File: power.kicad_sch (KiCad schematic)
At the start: 10 parts

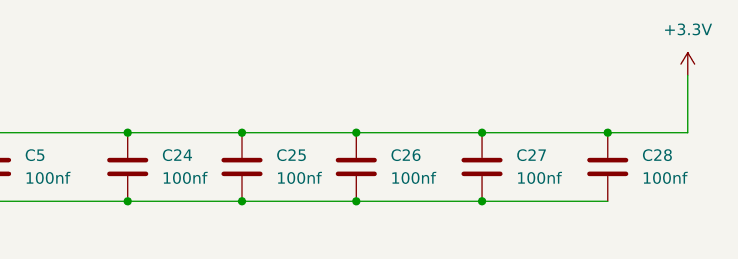
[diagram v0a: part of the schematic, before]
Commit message: feat: PCB layout updates, schematic changes, fp-lib-table config
- cnc_pic32.kicad_pcb: component repositioning, board outline, text formatting
- cnc_pic32.kicad_prl/pro: project settings updates
- fp-lib-table: add Library path to Library.pretty
- mcu.kicad_sch: PIC32 pin configuration updates
- zigbee.kicad_sch: MRF24J40 module updates
- oscilator.kicad_sch: crystal configuration
- power.kicad_sch/power_ft232.kicad_sch: power supply updates
- oled.kicad_sch: OLED display connections
- idc.kicad_sch: IDC connector updates
- osc_ft232.kicad_sch: FT232 crystal
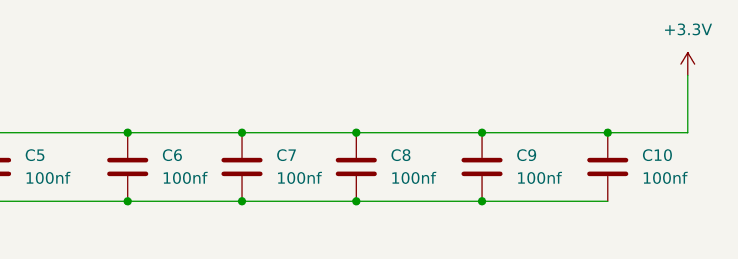
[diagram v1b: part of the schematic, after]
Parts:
- renumbered C28 to C10, C24 to C6, C25 to C7, C26 to C8, C27 to C9
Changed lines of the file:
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@@
 		(dnp no)
 		(fields_autoplaced yes)
-		(property "Reference" "C27"
+		(property "Reference" "C9"
 			(at 177.8 63.5 0)
 			(show_name no)
@@
 			(project "cnc_pic32"
 				(path "/13dbfc1f-be47-44ca-9042-3d6a9a657d7d/8e42f8aa-f00a-41b2-96fb-3753b4f2b509"
-					(reference "C27")
+					(reference "C9")
 					(unit 1)
 				)
@@
 		(dnp no)
 		(fields_autoplaced yes)
-		(property "Reference" "C24"
+		(property "Reference" "C6"
 			(at 138.43 63.5 0)
 			(show_name no)
@@
 			(project "cnc_pic32"
 				(path "/13dbfc1f-be47-44ca-9042-3d6a9a657d7d/8e42f8aa-f00a-41b2-96fb-3753b4f2b509"
-					(reference "C24")
+					(reference "C6")
 					(unit 1)
 				)
@@
 		(in_pos_files yes)
 		(dnp no)
-		(property "Reference" "#PWR040"
+		(property "Reference" "#PWR04"
 			(at 57.15 74.93 0)
 			(hide yes)
@@
 			(project "cnc_pic32"
 				(path "/13dbfc1f-be47-44ca-9042-3d6a9a657d7d/8e42f8aa-f00a-41b2-96fb-3753b4f2b509"
-					(reference "#PWR040")
+					(reference "#PWR04")
 					(unit 1)
 				)
@@
 		(dnp no)
 		(fields_autoplaced yes)
-		(property "Reference" "C26"
+		(property "Reference" "C8"
 			(at 163.83 63.5 0)
 			(show_name no)
@@
 			(project "cnc_pic32"
 				(path "/13dbfc1f-be47-44ca-9042-3d6a9a657d7d/8e42f8aa-f00a-41b2-96fb-3753b4f2b509"
-					(reference "C26")
+					(reference "C8")
 					(unit 1)
 				)
@@
 		(dnp no)
 		(fields_autoplaced yes)
-		(property "Reference" "#PWR039"
+		(property "Reference" "#PWR05"
 			(at 196.85 58.42 0)
 			(hide yes)
@@
 			(project "cnc_pic32"
 				(path "/13dbfc1f-be47-44ca-9042-3d6a9a657d7d/8e42f8aa-f00a-41b2-96fb-3753b4f2b509"
-					(reference "#PWR039")
+					(reference "#PWR05")
 					(unit 1)
 				)
@@
 		(dnp no)
 		(fields_autoplaced yes)
-		(property "Reference" "C25"
+		(property "Reference" "C7"
 			(at 151.13 63.5 0)
 			(show_name no)
@@
 			(project "cnc_pic32"
 				(path "/13dbfc1f-be47-44ca-9042-3d6a9a657d7d/8e42f8aa-f00a-41b2-96fb-3753b4f2b509"
-					(reference "C25")
+					(reference "C7")
 					(unit 1)
 				)
@@
 		(dnp no)
 		(fields_autoplaced yes)
-		(property "Reference" "C28"
+		(property "Reference" "C10"
 			(at 191.77 63.5 0)
 			(show_name no)
@@
 			(project "cnc_pic32"
 				(path "/13dbfc1f-be47-44ca-9042-3d6a9a657d7d/8e42f8aa-f00a-41b2-96fb-3753b4f2b509"
-					(reference "C28")
-					(unit 1)
-				)
+					(reference "C10")
+					(unit 1)
+				)

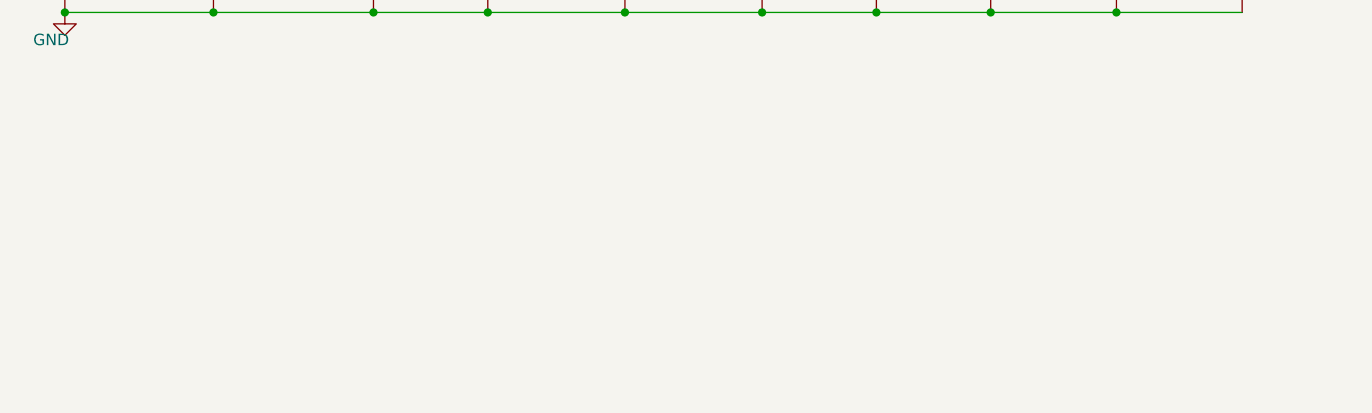
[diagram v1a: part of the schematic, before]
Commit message: feat: add orphaned PCB components to schematics - R4/R5 MCU, R41/R42 OLED, C37/C38 power
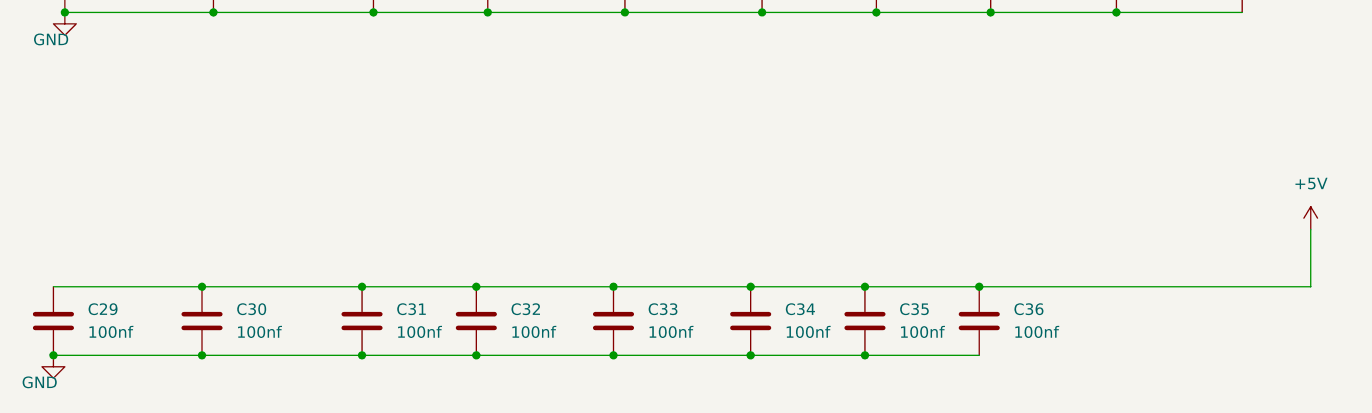
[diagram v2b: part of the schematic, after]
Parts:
- added C29, C30, C31, C32, C33, C34, C35, C36: 100nf, Capacitor_SMD:C_0805_2012Metric, symbol Device:C
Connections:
- net GND: now also C29.2, C30.2, C31.2, C32.2, C33.2, C34.2, C35.2, C36.2
- new net +5V: C29.1, C30.1, C31.1, C32.1, C33.1, C34.1, C35.1, C36.1

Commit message: feat: PCB layout updates, schematic changes, remove freerouting.dsn
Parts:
- removed C30: 100nf, Capacitor_SMD:C_0805_2012Metric, symbol Device:C
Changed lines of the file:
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@@
-	)
-	(junction
-		(at 72.39 106.68)
-		(diameter 0)
-		(color 0 0 0 0)
 	)
 	(junction
@@
 	)
 	(junction
-		(at 72.39 99.06)
-		(diameter 0)
-		(color 0 0 0 0)
-	)
-	(junction
 		(at 187.96 60.96)
 		(diameter 0)
@@
 	(wire
 		(pts
-			(xy 72.39 106.68) (xy 90.17 106.68)
+			(xy 55.88 106.68) (xy 90.17 106.68)
 		)
 		(stroke
@@
 	(wire
 		(pts
-			(xy 72.39 99.06) (xy 90.17 99.06)
+			(xy 55.88 99.06) (xy 90.17 99.06)
 		)
 		(stroke
@@
 	(wire
 		(pts
-			(xy 55.88 99.06) (xy 72.39 99.06)
-		)
-		(stroke
-			(width 0)
-			(type default)
-		)
-	)
-	(wire
-		(pts
 			(xy 73.66 60.96) (xy 91.44 60.96)
-		)
-		(stroke
-			(width 0)
-			(type default)
-		)
-	)
-	(wire
-		(pts
-			(xy 55.88 106.68) (xy 72.39 106.68)
 		)
 		(stroke
@@
 					(unit 1)
 				)
-			)
-		)
-	)
-	(symbol
-		(lib_name "C_1")
-		(lib_id "Device:C")
-		(at 72.39 102.87 0)
-		(unit 1)
-		(body_style 1)
-		(exclude_from_sim no)
-		(in_bom yes)
-		(on_board yes)
-		(in_pos_files yes)
-		(dnp no)
-		(fields_autoplaced yes)
-		(property "Reference" "C30"
-			(at 76.2 101.5999 0)
-			(show_name no)
-			(do_not_autoplace no)
-			(effects
-				(font
-					(size 1.27 1.27)
-				)
-				(justify left)
-			)
-		)
-		(property "Value" "100nf"
-			(at 76.2 104.1399 0)
-			(show_name no)
-			(do_not_autoplace no)
-			(effects
-				(font
-					(size 1.27 1.27)
-				)
-				(justify left)
-			)
-		)
-		(property "Footprint" "Capacitor_SMD:C_0805_2012Metric"
-			(at 73.3552 106.68 0)
-			(hide yes)
-			(show_name no)
-			(do_not_autoplace no)
-			(effects
-				(font
-					(size 1.27 1.27)
-				)
-			)
-		)
-		(property "Datasheet" ""
-			(at 72.39 102.87 0)
-			(hide yes)
-			(show_name no)
-			(do_not_autoplace no)
-			(effects
-				(font
-					(size 1.27 1.27)
-				)
-			)
-		)
-		(property "Description" ""
-			(at 72.39 102.87 0)
-			(show_name no)
-			(do_not_autoplace no)
-			(effects
-				(font
-					(size 1.27 1.27)
-				)
-			)
-		)
-		(pin "1"
-		)
-		(pin "2"
-		)
-		(instances
-			(project "cnc_pic32"
-				(path "/13dbfc1f-be47-44ca-9042-3d6a9a657d7d/8e42f8aa-f00a-41b2-96fb-3753b4f2b509"
-					(reference "C30")
-					(unit 1)
-				)

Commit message: feat: 2-layer stackup, bus net class and schematic cleanup
PCB / project
- Reduce board from 4 layers to 2 (F.Cu / B.Cu) for cheaper fabrication
- Add "bus" net class and reorder net class priorities (bus 0, usb_differential 1, ...)

Schematics
- usb_conector_Ft232: add D+ / D-- labels on the USB mini-B data pair
- ft232: add 10K pull-ups, 100nf decoupling and test points on +3.3VA
- tp_ft232: remove solder jumpers JP1/JP2 (TX_Rpi / RX_Rpi now direct)
- Usb_pic32: add C38 100nf decoupling on +5V
- oled: expand connector J25 from 7 to 8 pins
- mcu / idc / power / zigbee / buttons / cnc_pic32: annotation and net cleanup

docs
- Add USB-Mini-B pinout reference images
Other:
- moved on the sheet: C29
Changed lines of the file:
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@@
+	)
+	(junction
+		(at 90.17 99.06)
+		(diameter 0)
+		(color 0 0 0 0)
 	)
 	(junction
@@
 	)
 	(junction
-		(at 55.88 106.68)
-		(diameter 0)
-		(color 0 0 0 0)
-	)
-	(junction
 		(at 173.99 68.58)
 		(diameter 0)
@@
 	)
 	(junction
-		(at 90.17 99.06)
-		(diameter 0)
-		(color 0 0 0 0)
-	)
-	(junction
 		(at 102.87 99.06)
 		(diameter 0)
@@
 	)
 	(junction
+		(at 76.2 106.68)
+		(diameter 0)
+		(color 0 0 0 0)
+	)
+	(junction
 		(at 187.96 60.96)
 		(diameter 0)
@@
 	(wire
 		(pts
-			(xy 55.88 106.68) (xy 90.17 106.68)
+			(xy 55.88 106.68) (xy 76.2 106.68)
 		)
 		(stroke
@@
 	(wire
 		(pts
+			(xy 76.2 106.68) (xy 90.17 106.68)
+		)
+		(stroke
+			(width 0)
+			(type default)
+		)
+	)
+	(wire
+		(pts
 			(xy 102.87 99.06) (xy 118.11 99.06)
 		)
@@
 	(wire
 		(pts
-			(xy 55.88 99.06) (xy 90.17 99.06)
+			(xy 76.2 99.06) (xy 90.17 99.06)
 		)
 		(stroke
@@
 		(lib_name "C_1")
 		(lib_id "Device:C")
-		(at 55.88 102.87 0)
+		(at 76.2 102.87 0)
 		(unit 1)
 		(body_style 1)
@@
 		(fields_autoplaced yes)
 		(property "Reference" "C29"
-			(at 59.69 101.5999 0)
+			(at 80.01 101.5999 0)
 			(show_name no)
 			(do_not_autoplace no)
@@
 		)
 		(property "Value" "100nf"
-			(at 59.69 104.1399 0)
+			(at 80.01 104.1399 0)
 			(show_name no)
 			(do_not_autoplace no)
@@
 		)
 		(property "Footprint" "Capacitor_SMD:C_0805_2012Metric"
-			(at 56.8452 106.68 0)
+			(at 77.1652 106.68 0)
 			(hide yes)
 			(show_name no)
@@
 		)
 		(property "Datasheet" ""
-			(at 55.88 102.87 0)
+			(at 76.2 102.87 0)
 			(hide yes)
 			(show_name no)
@@
 		)
 		(property "Description" ""
-			(at 55.88 102.87 0)
-			(show_name no)
-			(do_not_autoplace no)
+			(at 76.2 102.87 0)
+			(show_name no)
+			(do_not_autoplace no)

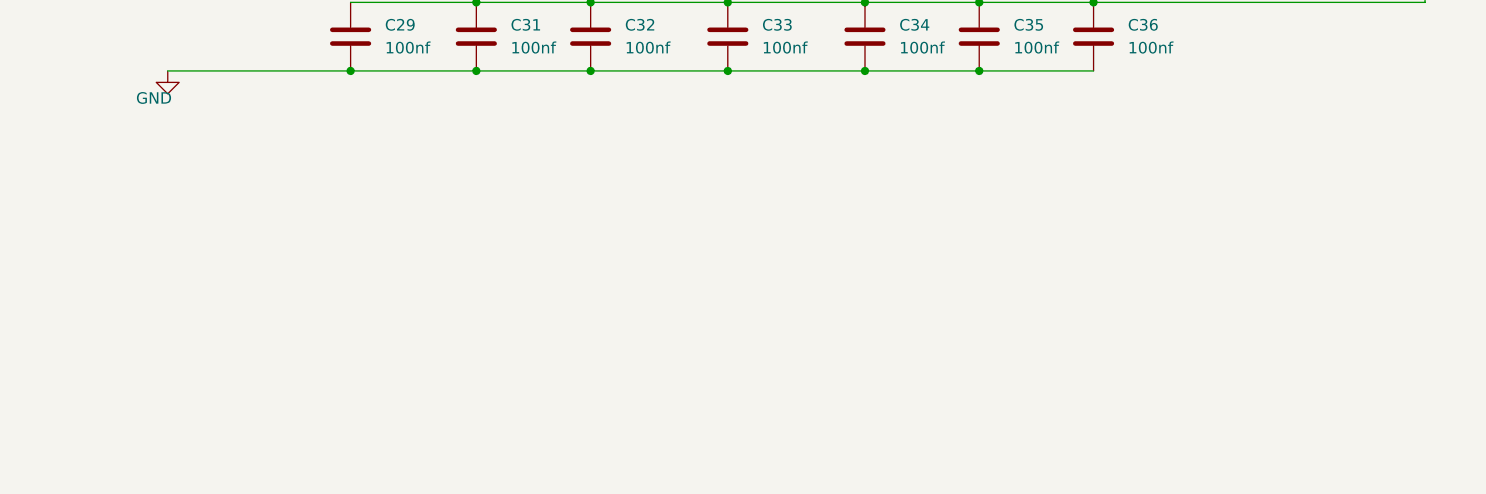
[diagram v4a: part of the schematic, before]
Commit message: feat: add MA240011 module sheet with labeled pins + Altium socket footprint
Esquemático
- Nueva hoja hija MA240011.kicad_sch (módulo PIC32 TQFP-100) referenciada
  desde la hoja MA240011 de mcu.kicad_sch
- mcu.kicad_sch: los 83 pines jerárquicos de MA240011 quedan rotulados con un
  label local del mismo nombre; 81 de ellos con un tramo de wire de 2.54 mm
  (un label solo no conecta a un pin de hoja) y RD4/RD5 sobre el wire existente
- mcu.kicad_sch: borde derecho del sheet 104.775 -> 106.68 mm y sus 41 pines,
  para quedar en grilla de 1.27 mm (evita 41 avisos endpoint_off_grid)
- ERC: 341 -> 158 violaciones; pin_not_connected 120 -> 39,
  isolated_pin_label 113 -> 10, endpoint_off_grid 6 -> 6
- power / zigbee / oled / pololu / cnc_pic32: pines MS1-MS3, conectores y
  anotacion de netnames

PCB
- Referencia de los 132 footprints a size 0.8 x 0.8 mm y thickness 0.12 mm
  (render_cache obsoleto eliminado para forzar el re-render)

Footprints
- lib/altium.pretty/MA240011_Socket_TQFP100_100pin.kicad_mod: zocalo adaptador
  de 100 pines TH pitch 1.27 mm convertido desde altium/Multimedia/MM20141127.PcbDoc
  (J4, patron MA240011); pads girados 90 grados sentido horario
- fp-lib-table: alta de la biblioteca "altium" (${KIPRJMOD}/lib/altium.pretty)

.gitignore
- Ignorar altium/, tmp/ y *.bkp (backups de KiCad)
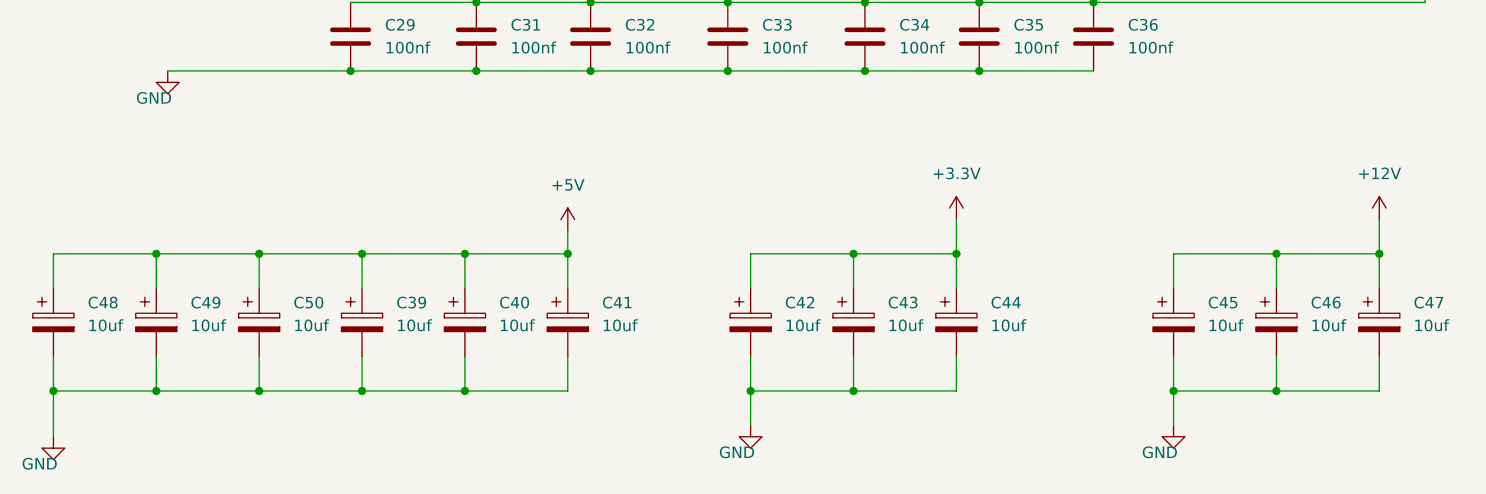
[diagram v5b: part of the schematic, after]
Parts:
- added C39, C40, C41, C42, C43, C44, C45, C46, C47, C48, C49, C50: 10uf, Capacitor_SMD:C_Elec_6.3x5.4, symbol Device:C_Polarized
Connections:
- net +3.3V: now also C42.1, C43.1, C44.1
- net +5V: now also C39.1, C40.1, C41.1, C48.1, C49.1, C50.1
- net GND: now also C39.2, C40.2, C41.2, C42.2, C43.2, C44.2, C45.2, C46.2, C47.2, C48.2, C49.2, C50.2
- new net +12V: C45.1, C46.1, C47.1

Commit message: add files
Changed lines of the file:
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@@
 	)
 	(junction
-		(at 167.64 142.24)
+		(at 167.64 127)
 		(diameter 0)
 		(color 0 0 0 0)
 	)
 	(junction
-		(at 57.15 68.58)
+		(at 167.64 142.24)
 		(diameter 0)
 		(color 0 0 0 0)
@@
 	)
 	(junction
-		(at 76.2 106.68)
-		(diameter 0)
-		(color 0 0 0 0)
-	)
-	(junction
 		(at 187.96 60.96)
 		(diameter 0)
@@
 	)
 	(junction
+		(at 76.2 106.68)
+		(diameter 0)
+		(color 0 0 0 0)
+	)
+	(junction
+		(at 57.15 68.58)
+		(diameter 0)
+		(color 0 0 0 0)
+	)
+	(junction
 		(at 173.99 60.96)
 		(diameter 0)
@@
 	(wire
 		(pts
-			(xy 195.58 92.71) (xy 195.58 99.06)
+			(xy 158.75 92.71) (xy 158.75 99.06)
 		)
 		(stroke
@@
 	(wire
 		(pts
-			(xy 55.88 106.68) (xy 76.2 106.68)
+			(xy 190.5 142.24) (xy 179.07 142.24)
 		)
 		(stroke
@@
 	(wire
 		(pts
-			(xy 190.5 142.24) (xy 179.07 142.24)
+			(xy 133.35 106.68) (xy 146.05 106.68)
 		)
 		(stroke
@@
 	(wire
 		(pts
-			(xy 133.35 106.68) (xy 146.05 106.68)
+			(xy 88.9 138.43) (xy 88.9 142.24)
 		)
 		(stroke
@@
 	(wire
 		(pts
-			(xy 88.9 138.43) (xy 88.9 142.24)
+			(xy 76.2 110.49) (xy 76.2 106.68)
 		)
 		(stroke
@@
 	(wire
 		(pts
+			(xy 57.15 73.66) (xy 57.15 68.58)
+		)
+		(stroke
+			(width 0)
+			(type default)
+		)
+	)
+	(wire
+		(pts
 			(xy 102.87 99.06) (xy 118.11 99.06)
 		)
@@
 	(wire
 		(pts
-			(xy 158.75 99.06) (xy 195.58 99.06)
-		)
-		(stroke
-			(width 0)
-			(type default)
-		)
-	)
-	(wire
-		(pts
 			(xy 120.65 127) (xy 132.08 127)
 		)
@@
 	(symbol
 		(lib_id "power:+5V")
-		(at 195.58 92.71 0)
+		(at 158.75 92.71 0)
 		(unit 1)
 		(body_style 1)
@@
 		(fields_autoplaced yes)
 		(property "Reference" "#PWR081"
-			(at 195.58 96.52 0)
+			(at 158.75 96.52 0)
 			(hide yes)
 			(show_name no)
@@
 		)
 		(property "Value" "+5V"
-			(at 195.58 87.63 0)
+			(at 158.75 87.63 0)
 			(show_name no)
 			(do_not_autoplace no)
@@
 		)
 		(property "Footprint" ""
-			(at 195.58 92.71 0)
+			(at 158.75 92.71 0)
 			(hide yes)
 			(show_name no)
@@
 		)
 		(property "Datasheet" ""
-			(at 195.58 92.71 0)
+			(at 158.75 92.71 0)
 			(hide yes)
 			(show_name no)
@@
 		)
 		(property "Description" "Power symbol creates a global label with name \"+5V\""
-			(at 195.58 92.71 0)
+			(at 158.75 92.71 0)
 			(hide yes)
 			(show_name no)
@@
 	(symbol
 		(lib_id "power:GND")
-		(at 55.88 106.68 0)
+		(at 76.2 110.49 0)
 		(unit 1)
 		(body_style 1)
@@
 		(dnp no)
 		(property "Reference" "#PWR080"
-			(at 55.88 113.03 0)
+			(at 76.2 116.84 0)
 			(hide yes)
 			(show_name no)
@@
 		)
 		(property "Value" "GND"
-			(at 54.356 109.728 0)
+			(at 74.676 113.538 0)
 			(show_name no)
 			(do_not_autoplace no)
@@
 		)
 		(property "Footprint" ""
-			(at 55.88 106.68 0)
+			(at 76.2 110.49 0)
 			(hide yes)
 			(show_name no)
@@
 		)
 		(property "Datasheet" ""
-			(at 55.88 106.68 0)
+			(at 76.2 110.49 0)
 			(hide yes)
 			(show_name no)
@@
 		)
 		(property "Description" "Power symbol creates a global label with name \"GND\" , ground"
-			(at 55.88 106.68 0)
+			(at 76.2 110.49 0)
 			(hide yes)
 			(show_name no)
@@
 	(symbol
 		(lib_id "power:GND")
-		(at 57.15 68.58 0)
+		(at 57.15 73.66 0)
 		(unit 1)
 		(body_style 1)
@@
 		(dnp no)
 		(property "Reference" "#PWR04"
-			(at 57.15 74.93 0)
+			(at 57.15 80.01 0)
 			(hide yes)
 			(show_name no)
@@
 		)
 		(property "Value" "GND"
-			(at 55.626 71.628 0)
+			(at 55.372 78.74 0)
 			(show_name no)
 			(do_not_autoplace no)
@@
 		)
 		(property "Footprint" ""
-			(at 57.15 68.58 0)
+			(at 57.15 73.66 0)
 			(hide yes)
 			(show_name no)
@@
 		)
 		(property "Datasheet" ""
-			(at 57.15 68.58 0)
+			(at 57.15 73.66 0)
 			(hide yes)
 			(show_name no)
@@
 		)
 		(property "Description" "Power symbol creates a global label with name \"GND\" , ground"
-			(at 57.15 68.58 0)
+			(at 57.15 73.66 0)
 			(hide yes)
 			(show_name no)
@@
 					(unit 1)
 				)
+			)
+		)
+	)
+	(symbol
+		(lib_id "power:PWR_FLAG")
+		(at 167.64 127 0)
+		(unit 1)
+		(body_style 1)
+		(exclude_from_sim no)
+		(in_bom yes)
+		(on_board yes)
+		(in_pos_files yes)
+		(dnp no)
+		(fields_autoplaced yes)
+		(property "Reference" "#FLG01"
+			(at 167.64 125.095 0)
+			(hide yes)
+			(show_name no)
+			(do_not_autoplace no)
+			(effects
+				(font
+					(size 1.27 1.27)
+				)
+			)
+		)
+		(property "Value" "PWR_FLAG"
+			(at 167.64 121.92 0)
+			(show_name no)
+			(do_not_autoplace no)
+			(effects
+				(font
+					(size 1.27 1.27)
+				)
+			)
+		)
+		(property "Footprint" ""
+			(at 167.64 127 0)
+			(hide yes)
+			(show_name no)
+			(do_not_autoplace no)
+			(effects
+				(font
+					(size 1.27 1.27)
+				)
+			)
+		)
+		(property "Datasheet" ""
+			(at 167.64 127 0)
+			(hide yes)
+			(show_name no)
+			(do_not_autoplace no)
+			(effects
+				(font
+					(size 1.27 1.27)
+				)
+			)
+		)
+		(property "Description" "Special symbol for telling ERC where power comes from"
+			(at 167.64 127 0)
+			(hide yes)
+			(show_name no)
+			(do_not_autoplace no)
+			(effects
+				(font
+					(size 1.27 1.27)
+				)
+			)
+		)
+		(pin "1"
+		)
+		(instances
+			(project "cnc_pic32"
+				(path "/13dbfc1f-be47-44ca-9042-3d6a9a657d7d/8e42f8aa-f00a-41b2-96fb-3753b4f2b509"
+					(reference "#FLG01")
+					(unit 1)
+				)

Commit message: updated
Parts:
- removed C44, C46: 10uf, Capacitor_SMD:C_Elec_6.3x5.4, symbol Device:C_Polarized
- added C44, C53, C54, C55, C56, C57, C58, C59, C60: 100nf, Capacitor_SMD:C_0805_2012Metric, symbol Device:C
- added C51, C52: EFVH035ADA100M0454, Capacitor_SMD:C_Elec_5x5.4, symbol Device:C_Polarized
- C10, C3, C4, C9: footprint Capacitor_SMD:C_0805_2012Metric -> Resistor_SMD:R_0603_1608Metric
- C36: value 100nf -> 4.7uf
- C39, C40, C41, C48, C49, C50: value 10uf -> RVT100UF35V67RV0034
- C42, C43, C45, C47: value 10uf -> EFVH035ADA100M0454; footprint Capacitor_SMD:C_Elec_6.3x5.4 -> Capacitor_SMD:C_Elec_5x5.4
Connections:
- net +12V is gone; now on net +3.3V: C45.1, C47.1
- net +3.3V: now also C44.1, C51.1, C52.1, C53.1, C54.1, C55.1, C56.1
- net GND: now also C44.2, C51.2, C52.2, C53.2, C54.2, C55.2, C56.2, C57.2, C58.2, C59.2, C60.2
- net +5V renamed VCC
- net VCC: now also C57.1, C58.1, C59.1, C60.1
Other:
- moved on the sheet: C45
